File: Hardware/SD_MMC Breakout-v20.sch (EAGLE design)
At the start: 8 parts, among them U1 SD_CARD_SOCKET4UCON

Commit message: Added standoffs, sch work
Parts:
- added FRAME1: FRAME-LETTER, SparkFun-Aesthetics:FRAME-LETTER
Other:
- note added: "A. Weiss"
- note added: "Revised by: Patrick Alberts"
- note added: "v21"
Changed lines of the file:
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@@
 <?xml version="1.0" encoding="utf-8"?>
 <!DOCTYPE eagle SYSTEM "eagle.dtd">
-<eagle version="6.4">
+<eagle version="6.5.0">
 <drawing>
 <settings>
@@
 <layer number="106" name="bPlate" color="7" fill="1" visible="no" active="yes"/>
 <layer number="107" name="Crop" color="7" fill="1" visible="no" active="yes"/>
+<layer number="108" name="tplace-old" color="10" fill="1" visible="no" active="yes"/>
+<layer number="109" name="ref-old" color="11" fill="1" visible="no" active="yes"/>
 <layer number="116" name="Patch_BOT" color="9" fill="4" visible="yes" active="yes"/>
 <layer number="121" name="_tsilk" color="7" fill="1" visible="yes" active="yes"/>
@@
 <layer number="144" name="Drill_legend" color="7" fill="1" visible="no" active="yes"/>
 <layer number="151" name="HeatSink" color="7" fill="1" visible="yes" active="yes"/>
+<layer number="199" name="Contour" color="7" fill="1" visible="yes" active="yes"/>
 <layer number="200" name="200bmp" color="1" fill="10" visible="no" active="no"/>
 <layer number="201" name="201bmp" color="2" fill="1" visible="no" active="no"/>
@@
 </classes>
 <parts>
-<part name="FRAME1" library="SparkFun" deviceset="FRAME-LETTER" device=""/>
+<part name="FRAME1" library="SparkFun-Aesthetics" deviceset="FRAME-LETTER" device=""/>
 <part name="U$1" library="SparkFun" deviceset="LOGO-SFE" device="NEW"/>
 <part name="U1" library="SparkFun-Connectors" deviceset="SD_CARD_SOCKET" device="4UCON"/>
@@
 <text x="2.54" y="177.8" size="1.778" layer="97">v20: new SD socket, extra pin holes, standoffs</text>
 <text x="68.58" y="88.9" size="1.778" layer="97">extra pins</text>
+<text x="166.116" y="11.684" size="2.54" layer="94">A. Weiss</text>
+<text x="149.606" y="6.604" size="2.54" layer="94">Revised by: Patrick Alberts</text>
+<text x="238.76" y="7.62" size="2.54" layer="94">v21</text>
 </plain>
 <instances>
 <instance part="FRAME1" gate="G$1" x="0" y="0"/>
 <instance part="FRAME1" gate="G$2" x="147.32" y="0"/>
-<instance part="U$1" gate="G$1" x="154.94" y="27.94"/>
+<instance part="U$1" gate="G$1" x="236.22" y="43.18"/>
 <instance part="U1" gate="G$1" x="152.4" y="109.22" smashed="yes">
 <attribute name="NAME" x="145.034" y="127.508" size="1.778" layer="95"/>
@@
 <instance part="U$3" gate="G$1" x="132.08" y="10.16"/>
 <instance part="JP5" gate="G$1" x="93.98" y="116.84"/>
-<instance part="JP2" gate="G$1" x="170.18" y="30.48"/>
-<instance part="JP3" gate="G$1" x="175.26" y="30.48"/>
+<instance part="JP2" gate="G$1" x="218.44" y="43.18"/>
+<instance part="JP3" gate="G$1" x="223.52" y="43.18"/>
 </instances>
 <busses>
@@
 <segment>
 <pinref part="U1" gate="G$1" pin="CD"/>
-<wire x1="132.08" y1="106.68" x2="139.7" y2="106.68" width="0.1524" layer="91"/>
-<label x="132.08" y="106.68" size="1.778" layer="95"/>
-</segment>
-<segment>
-<wire x1="104.14" y1="114.3" x2="114.3" y2="114.3" width="0.1524" layer="91"/>
-<label x="109.22" y="114.3" size="1.778" layer="95"/>
+<wire x1="137.16" y1="106.68" x2="139.7" y2="106.68" width="0.1524" layer="91"/>
+<label x="137.16" y="106.68" size="1.27" layer="95" rot="R180" xref="yes"/>
+</segment>
+<segment>
+<wire x1="104.14" y1="114.3" x2="109.22" y2="114.3" width="0.1524" layer="91"/>
 <pinref part="JP5" gate="G$1" pin="7"/>
+<label x="109.22" y="114.3" size="1.27" layer="95" xref="yes"/>
 </segment>
 </net>
@@
 <segment>
 <pinref part="U1" gate="G$1" pin="CMD"/>
-<wire x1="132.08" y1="111.76" x2="139.7" y2="111.76" width="0.1524" layer="91"/>
-<label x="132.08" y="111.76" size="1.778" layer="95"/>
-</segment>
-<segment>
-<wire x1="104.14" y1="116.84" x2="114.3" y2="116.84" width="0.1524" layer="91"/>
-<label x="109.22" y="116.84" size="1.778" layer="95"/>
+<wire x1="137.16" y1="111.76" x2="139.7" y2="111.76" width="0.1524" layer="91"/>
+<label x="137.16" y="111.76" size="1.27" layer="95" rot="R180" xref="yes"/>
+</segment>
+<segment>
+<wire x1="104.14" y1="116.84" x2="109.22" y2="116.84" width="0.1524" layer="91"/>
 <pinref part="JP5" gate="G$1" pin="8"/>
+<label x="109.22" y="116.84" size="1.27" layer="95" xref="yes"/>
 </segment>
 </net>
@@
 <segment>
 <pinref part="U1" gate="G$1" pin="CLK"/>
-<wire x1="132.08" y1="114.3" x2="139.7" y2="114.3" width="0.1524" layer="91"/>
-<label x="132.08" y="114.3" size="1.778" layer="95"/>
-</segment>
-<segment>
-<wire x1="104.14" y1="111.76" x2="114.3" y2="111.76" width="0.1524" layer="91"/>
-<label x="109.22" y="111.76" size="1.778" layer="95"/>
+<wire x1="137.16" y1="114.3" x2="139.7" y2="114.3" width="0.1524" layer="91"/>
+<label x="137.16" y="114.3" size="1.27" layer="95" rot="R180" xref="yes"/>
+</segment>
+<segment>
+<wire x1="104.14" y1="111.76" x2="109.22" y2="111.76" width="0.1524" layer="91"/>
 <pinref part="JP5" gate="G$1" pin="6"/>
+<label x="109.22" y="111.76" size="1.27" layer="95" xref="yes"/>
 </segment>
 </net>
@@
 <segment>
 <pinref part="U1" gate="G$1" pin="DAT1"/>
-<wire x1="132.08" y1="119.38" x2="139.7" y2="119.38" width="0.1524" layer="91"/>
-<label x="132.08" y="119.38" size="1.778" layer="95"/>
-</segment>
-<segment>
-<wire x1="104.14" y1="101.6" x2="114.3" y2="101.6" width="0.1524" layer="91"/>
-<label x="109.22" y="101.6" size="1.778" layer="95"/>
+<wire x1="137.16" y1="119.38" x2="139.7" y2="119.38" width="0.1524" layer="91"/>
+<label x="137.16" y="119.38" size="1.27" layer="95" rot="R180" xref="yes"/>
+</segment>
+<segment>
+<wire x1="104.14" y1="101.6" x2="109.22" y2="101.6" width="0.1524" layer="91"/>
 <pinref part="JP5" gate="G$1" pin="2"/>
+<label x="109.22" y="101.6" size="1.27" layer="95" xref="yes"/>
 </segment>
 </net>
@@
 <segment>
 <pinref part="U1" gate="G$1" pin="DAT0"/>
-<wire x1="132.08" y1="121.92" x2="139.7" y2="121.92" width="0.1524" layer="91"/>
-<label x="132.08" y="121.92" size="1.778" layer="95"/>
-</segment>
-<segment>
-<wire x1="104.14" y1="104.14" x2="114.3" y2="104.14" width="0.1524" layer="91"/>
-<label x="109.22" y="104.14" size="1.778" layer="95"/>
+<wire x1="137.16" y1="121.92" x2="139.7" y2="121.92" width="0.1524" layer="91"/>
+<label x="137.16" y="121.92" size="1.27" layer="95" rot="R180" xref="yes"/>
+</segment>
+<segment>
+<wire x1="104.14" y1="104.14" x2="109.22" y2="104.14" width="0.1524" layer="91"/>
 <pinref part="JP5" gate="G$1" pin="3"/>
+<label x="109.22" y="104.14" size="1.27" layer="95" xref="yes"/>
 </segment>
 </net>
@@
 <segment>
 <pinref part="U1" gate="G$1" pin="WP"/>
-<wire x1="139.7" y1="104.14" x2="132.08" y2="104.14" width="0.1524" layer="91"/>
-<label x="132.08" y="104.14" size="1.778" layer="95"/>
+<wire x1="139.7" y1="104.14" x2="137.16" y2="104.14" width="0.1524" layer="91"/>
+<label x="137.16" y="104.14" size="1.27" layer="95" rot="R180" xref="yes"/>
 </segment>
 <segment>
 <pinref part="JP5" gate="G$1" pin="1"/>
-<wire x1="104.14" y1="99.06" x2="114.3" y2="99.06" width="0.1524" layer="91"/>
-<label x="109.22" y="99.06" size="1.778" layer="95"/>
+<wire x1="104.14" y1="99.06" x2="109.22" y2="99.06" width="0.1524" layer="91"/>
+<label x="109.22" y="99.06" size="1.27" layer="95" xref="yes"/>
 </segment>
 </net>
@@
 <segment>
 <pinref part="U1" gate="G$1" pin="DAT2"/>
-<wire x1="132.08" y1="116.84" x2="139.7" y2="116.84" width="0.1524" layer="91"/>
-<label x="132.08" y="116.84" size="1.778" layer="95"/>
-</segment>
-<segment>
-<wire x1="104.14" y1="121.92" x2="114.3" y2="121.92" width="0.1524" layer="91"/>
-<label x="109.22" y="121.92" size="1.778" layer="95"/>
+<wire x1="137.16" y1="116.84" x2="139.7" y2="116.84" width="0.1524" layer="91"/>
+<label x="137.16" y="116.84" size="1.27" layer="95" rot="R180" xref="yes"/>
+</segment>
+<segment>
+<wire x1="104.14" y1="121.92" x2="109.22" y2="121.92" width="0.1524" layer="91"/>
 <pinref part="JP5" gate="G$1" pin="10"/>
+<label x="109.22" y="121.92" size="1.27" layer="95" xref="yes"/>
 </segment>
 </net>
@@
 <segment>
 <pinref part="U1" gate="G$1" pin="CD/DAT3"/>
-<wire x1="132.08" y1="109.22" x2="139.7" y2="109.22" width="0.1524" layer="91"/>
-<label x="132.08" y="109.22" size="1.778" layer="95"/>
-</segment>
-<segment>
-<wire x1="104.14" y1="119.38" x2="114.3" y2="119.38" width="0.1524" layer="91"/>
-<label x="109.22" y="119.38" size="1.778" layer="95"/>
+<wire x1="137.16" y1="109.22" x2="139.7" y2="109.22" width="0.1524" layer="91"/>
+<label x="137.16" y="109.22" size="1.27" layer="95" rot="R180" xref="yes"/>
+</segment>
+<segment>
+<wire x1="104.14" y1="119.38" x2="109.22" y2="119.38" width="0.1524" layer="91"/>
 <pinref part="JP5" gate="G$1" pin="9"/>
-</segment>
-</net>
+<label x="109.22" y="119.38" size="1.27" layer="95" xref="yes"/>
+</segment>
+</net>

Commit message: Updated Sch
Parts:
- removed U$2: CREATIVE_COMMONS, SparkFun-Aesthetics:CREATIVE_COMMONS
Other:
- note removed: "A.Weiss"
- note removed: "Revision Notes:"
- note removed: "v20: new SD socket, extra pin holes, standoffs"
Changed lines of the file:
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@@
 <part name="P+2" library="SparkFun-Aesthetics" deviceset="VCC" device=""/>
 <part name="GND2" library="SparkFun-Aesthetics" deviceset="GND" device=""/>
-<part name="U$2" library="SparkFun-Aesthetics" deviceset="CREATIVE_COMMONS" device=""/>
 <part name="U$3" library="SparkFun-Aesthetics" deviceset="OSHW-LOGO" device="S"/>
 <part name="JP5" library="SparkFun-Connectors" deviceset="M10" device="&quot;"/>
@@
 <sheet>
 <plain>
-<text x="22.86" y="5.08" size="1.778" layer="97">A.Weiss</text>
-<text x="2.54" y="180.34" size="1.778" layer="97">Revision Notes:</text>
-<text x="2.54" y="177.8" size="1.778" layer="97">v20: new SD socket, extra pin holes, standoffs</text>
 <text x="68.58" y="88.9" size="1.778" layer="97">extra pins</text>
 <text x="166.116" y="11.684" size="2.54" layer="94">A. Weiss</text>
@@
 <instance part="P+2" gate="1" x="106.68" y="127"/>
 <instance part="GND2" gate="1" x="106.68" y="93.98"/>
-<instance part="U$2" gate="G$1" x="5.08" y="5.08"/>
 <instance part="U$3" gate="G$1" x="132.08" y="10.16"/>
 <instance part="JP5" gate="G$1" x="93.98" y="116.84"/>

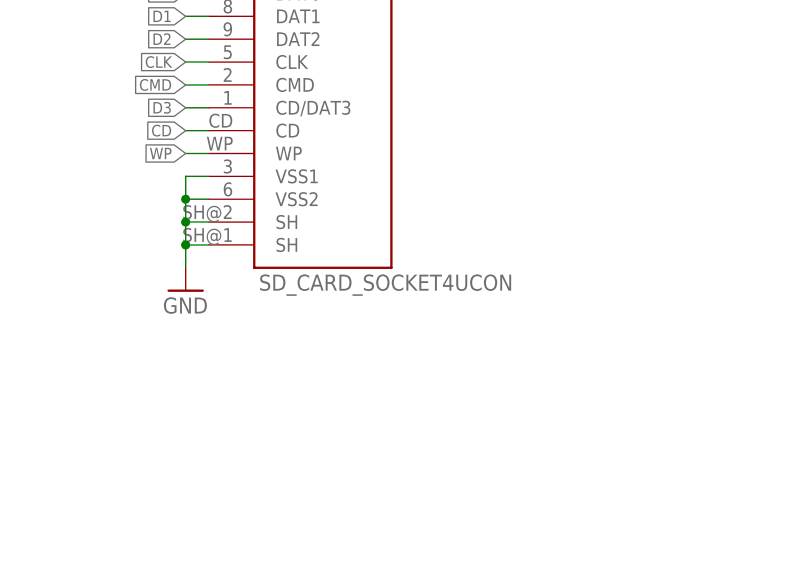
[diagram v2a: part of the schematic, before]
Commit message: added new sd socket
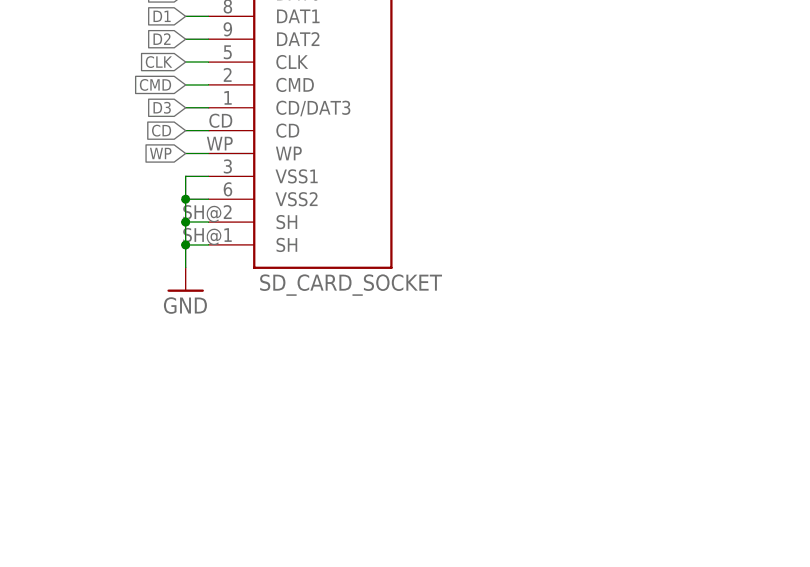
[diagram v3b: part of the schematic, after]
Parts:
- U1: value SD_CARD_SOCKET4UCON -> SD_CARD_SOCKET; device SparkFun-Connectors:SD_CARD_SOCKET4UCON -> SparkFun-Connectors:SD_CARD_SOCKET
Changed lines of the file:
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@@
 <?xml version="1.0" encoding="utf-8"?>
 <!DOCTYPE eagle SYSTEM "eagle.dtd">
-<eagle version="6.5.0">
+<eagle version="6.4">
 <drawing>
 <settings>
@@
 <layer number="108" name="tplace-old" color="10" fill="1" visible="no" active="yes"/>
 <layer number="109" name="ref-old" color="11" fill="1" visible="no" active="yes"/>
+<layer number="110" name="fp0" color="7" fill="1" visible="yes" active="yes"/>
+<layer number="111" name="LPC17xx" color="7" fill="1" visible="yes" active="yes"/>
+<layer number="112" name="tSilk" color="7" fill="1" visible="yes" active="yes"/>
+<layer number="113" name="IDFDebug" color="4" fill="1" visible="yes" active="yes"/>
 <layer number="116" name="Patch_BOT" color="9" fill="4" visible="yes" active="yes"/>
 <layer number="121" name="_tsilk" color="7" fill="1" visible="yes" active="yes"/>
 <layer number="122" name="_bsilk" color="7" fill="1" visible="yes" active="yes"/>
+<layer number="123" name="tTestmark" color="7" fill="1" visible="yes" active="yes"/>
+<layer number="124" name="bTestmark" color="7" fill="1" visible="yes" active="yes"/>
 <layer number="125" name="_tNames" color="7" fill="1" visible="no" active="yes"/>
+<layer number="126" name="_bNames" color="7" fill="1" visible="yes" active="yes"/>
+<layer number="127" name="_tValues" color="7" fill="1" visible="yes" active="yes"/>
+<layer number="128" name="_bValues" color="7" fill="1" visible="yes" active="yes"/>
+<layer number="131" name="tAdjust" color="7" fill="1" visible="yes" active="yes"/>
+<layer number="132" name="bAdjust" color="7" fill="1" visible="yes" active="yes"/>
 <layer number="144" name="Drill_legend" color="7" fill="1" visible="no" active="yes"/>
 <layer number="151" name="HeatSink" color="7" fill="1" visible="yes" active="yes"/>
+<layer number="152" name="_bDocu" color="7" fill="1" visible="yes" active="yes"/>
 <layer number="199" name="Contour" color="7" fill="1" visible="yes" active="yes"/>
 <layer number="200" name="200bmp" color="1" fill="10" visible="no" active="no"/>
@@
 <layer number="223" name="223bmp" color="24" fill="1" visible="no" active="no"/>
 <layer number="224" name="224bmp" color="25" fill="1" visible="no" active="no"/>
+<layer number="248" name="Housing" color="7" fill="1" visible="yes" active="yes"/>
+<layer number="249" name="Edge" color="7" fill="1" visible="yes" active="yes"/>
 <layer number="250" name="Descript" color="3" fill="1" visible="no" active="no"/>
 <layer number="251" name="SMDround" color="12" fill="11" visible="no" active="no"/>
@@
 <part name="FRAME1" library="SparkFun-Aesthetics" deviceset="FRAME-LETTER" device=""/>
 <part name="U$1" library="SparkFun" deviceset="LOGO-SFE" device="NEW"/>
-<part name="U1" library="SparkFun-Connectors" deviceset="SD_CARD_SOCKET" device="4UCON"/>
+<part name="U1" library="SparkFun-Connectors" deviceset="SD_CARD_SOCKET" device="" value="SD_CARD_SOCKET"/>
 <part name="JP1" library="SparkFun-Connectors" deviceset="M12" device="POGOPIN_HOLES_ONLY"/>
 <part name="GND1" library="SparkFun-Aesthetics" deviceset="GND" device=""/>

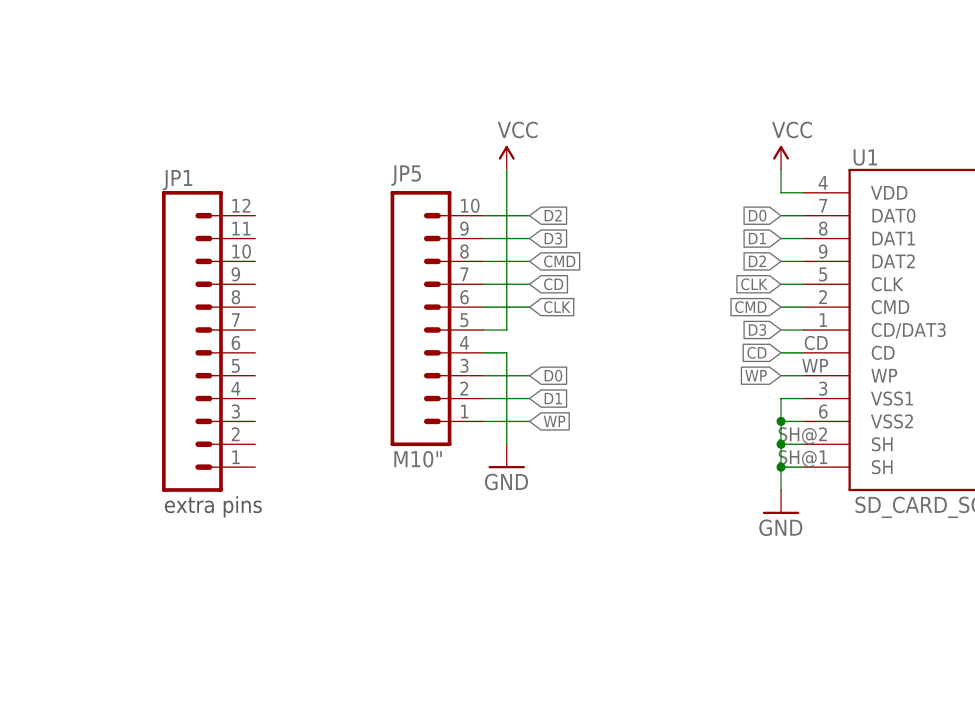
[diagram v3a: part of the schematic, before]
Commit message: Changed Font, Removed Extra Pins
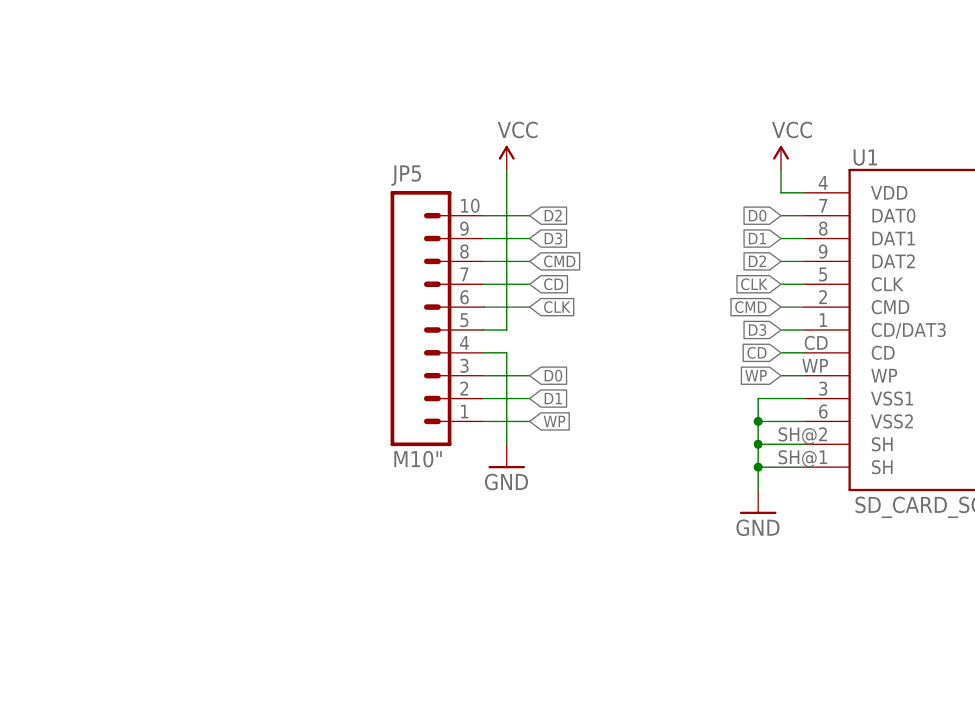
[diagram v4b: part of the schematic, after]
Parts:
- removed JP1: M12POGOPIN_HOLES_ONLY, SparkFun-Connectors:M12POGOPIN_HOLES_ONLY
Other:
- note removed: "extra pins"
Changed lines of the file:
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@@
 <part name="U$1" library="SparkFun" deviceset="LOGO-SFE" device="NEW"/>
 <part name="U1" library="SparkFun-Connectors" deviceset="SD_CARD_SOCKET" device="" value="SD_CARD_SOCKET"/>
-<part name="JP1" library="SparkFun-Connectors" deviceset="M12" device="POGOPIN_HOLES_ONLY"/>
 <part name="GND1" library="SparkFun-Aesthetics" deviceset="GND" device=""/>
 <part name="P+1" library="SparkFun-Aesthetics" deviceset="VCC" device=""/>
@@
 <sheet>
 <plain>
-<text x="68.58" y="88.9" size="1.778" layer="97">extra pins</text>
 <text x="166.116" y="11.684" size="2.54" layer="94">A. Weiss</text>
 <text x="149.606" y="6.604" size="2.54" layer="94">Revised by: Patrick Alberts</text>
@@
 <attribute name="VALUE" x="145.288" y="88.9" size="1.778" layer="96"/>
 </instance>
-<instance part="JP1" gate="G$1" x="68.58" y="109.22" smashed="yes">
-<attribute name="NAME" x="68.58" y="125.222" size="1.778" layer="95"/>
-</instance>
-<instance part="GND1" gate="1" x="137.16" y="88.9"/>
+<instance part="GND1" gate="1" x="134.62" y="88.9"/>
 <instance part="P+1" gate="1" x="137.16" y="127"/>
 <instance part="P+2" gate="1" x="106.68" y="127"/>
@@
 <segment>
 <pinref part="U1" gate="G$1" pin="VSS1"/>
-<wire x1="137.16" y1="101.6" x2="139.7" y2="101.6" width="0.1524" layer="91"/>
+<wire x1="134.62" y1="101.6" x2="139.7" y2="101.6" width="0.1524" layer="91"/>
 <pinref part="GND1" gate="1" pin="GND"/>
-<wire x1="137.16" y1="91.44" x2="137.16" y2="93.98" width="0.1524" layer="91"/>
+<wire x1="134.62" y1="91.44" x2="134.62" y2="93.98" width="0.1524" layer="91"/>
 <pinref part="U1" gate="G$1" pin="VSS2"/>
-<wire x1="137.16" y1="93.98" x2="137.16" y2="96.52" width="0.1524" layer="91"/>
-<wire x1="137.16" y1="96.52" x2="137.16" y2="99.06" width="0.1524" layer="91"/>
-<wire x1="137.16" y1="99.06" x2="137.16" y2="101.6" width="0.1524" layer="91"/>
-<wire x1="139.7" y1="99.06" x2="137.16" y2="99.06" width="0.1524" layer="91"/>
-<junction x="137.16" y="99.06"/>
+<wire x1="134.62" y1="93.98" x2="134.62" y2="96.52" width="0.1524" layer="91"/>
+<wire x1="134.62" y1="96.52" x2="134.62" y2="99.06" width="0.1524" layer="91"/>
+<wire x1="134.62" y1="99.06" x2="134.62" y2="101.6" width="0.1524" layer="91"/>
+<wire x1="139.7" y1="99.06" x2="134.62" y2="99.06" width="0.1524" layer="91"/>
+<junction x="134.62" y="99.06"/>
 <pinref part="U1" gate="G$1" pin="SH@2"/>
-<wire x1="139.7" y1="96.52" x2="137.16" y2="96.52" width="0.1524" layer="91"/>
-<junction x="137.16" y="96.52"/>
+<wire x1="139.7" y1="96.52" x2="134.62" y2="96.52" width="0.1524" layer="91"/>
+<junction x="134.62" y="96.52"/>
 <pinref part="U1" gate="G$1" pin="SH@1"/>
-<wire x1="139.7" y1="93.98" x2="137.16" y2="93.98" width="0.1524" layer="91"/>
-<junction x="137.16" y="93.98"/>
+<wire x1="139.7" y1="93.98" x2="134.62" y2="93.98" width="0.1524" layer="91"/>
+<junction x="134.62" y="93.98"/>
 </segment>
 <segment>
